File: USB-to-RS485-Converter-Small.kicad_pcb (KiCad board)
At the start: 4 copper layers, 71.5 x 33 mm, 21 parts, among them IC1 SN65HVD1782D, J1 Conn_01x02_Pin, J2 USB_B, J3 DE9_Plug_MountingHoles, U1 FT232RL

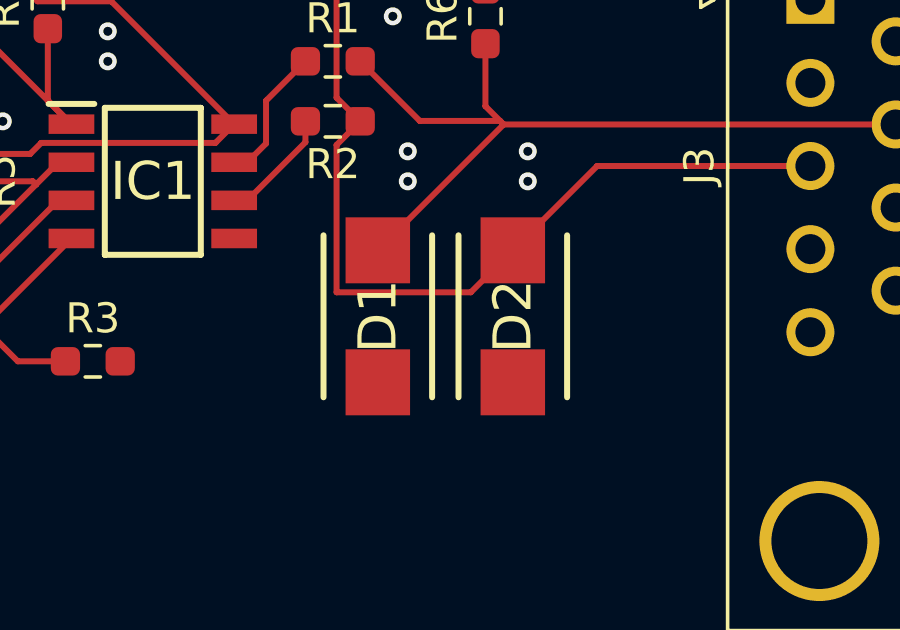
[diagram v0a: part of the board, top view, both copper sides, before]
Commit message: Changed TVS diode
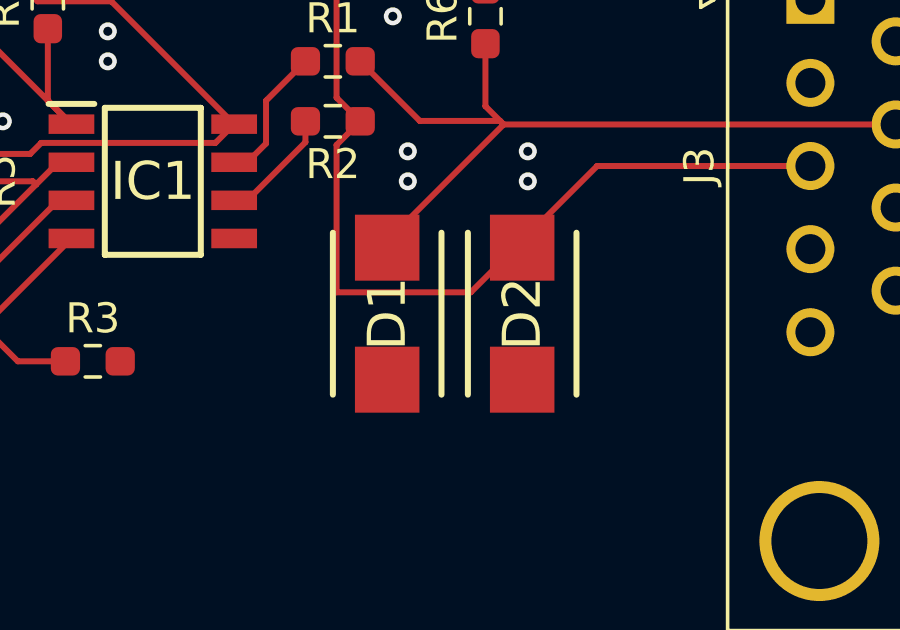
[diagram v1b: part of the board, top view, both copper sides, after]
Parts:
- D1, D2: value SMBJ43CA -> SMBJ7.0CA
- moved D1 0.32 mm to (158.0, 105.5)
- moved D2 0.32 mm to (162.5, 105.5), turned to -90 degrees
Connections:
- D2 pad 1: /GND -> Net-(J1-Pin_1)
- D2 pad 2: Net-(J1-Pin_1) -> /GND

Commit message: Changed RS485 transceiver and TVS diode
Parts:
- removed D1, D2: SMBJ7.0CA, SamacSys_Parts:DIONM5436X261N
- removed IC1: SN65HVD1782D, SamacSys_Parts:SOIC127P600X175-8N
- added D5: SM712_SOT23, Package_TO_SOT_SMD:SOT-23, F.Cu at (158.6, 105.4)
- added FL1: MCZ1210AH201CPTA0G, SamacSys_Parts:MCZ1210AH201CPTA0G, F.Cu at (166.5, 100.0)
- added U2: THVD1500, Package_SO:SOIC-8_3.9x4.9mm_P1.27mm, F.Cu at (150.0, 101.0)
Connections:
- J1 pad 1: Net-(J1-Pin_1) -> Net-(D5-A1)
- J3 pad 3: Net-(J1-Pin_1) -> Net-(FL1-Pad4)
- J3 pad 7: Net-(D1-Pad1) -> Net-(FL1-Pad3)
- R1 pad 2: Net-(D1-Pad1) -> Net-(D5-A2)
- R2 pad 1: Net-(J1-Pin_1) -> Net-(D5-A1)
- R6 pad 1: Net-(D1-Pad1) -> Net-(D5-A2)
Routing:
- net Net-(J1-Pin_1): track 35.6 -> 0.00 mm
- net Net-(D5-A1): track 0.00 -> 32.2 mm
- net Net-(D1-Pad1): track 27.4 -> 0.00 mm
- net Net-(D5-A2): track 0.00 -> 20.0 mm
- net Net-(FL1-Pad3): track 0.00 -> 10.2 mm
- net Net-(FL1-Pad4): track 0.00 -> 5.35 mm

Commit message: Removed choke filter
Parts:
- removed FL1: MCZ1210AH201CPTA0G, SamacSys_Parts:MCZ1210AH201CPTA0G
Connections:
- J3 pad 3: Net-(FL1-Pad4) -> Net-(D5-A1)
- J3 pad 7: Net-(FL1-Pad3) -> Net-(D5-A2)
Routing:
- net Net-(FL1-Pad3): track 10.2 -> 0.00 mm
- net Net-(D5-A2): track 20.0 -> 28.6 mm
- net Net-(FL1-Pad4): track 5.35 -> 0.00 mm
- net Net-(D5-A1): track 32.2 -> 36.5 mm
